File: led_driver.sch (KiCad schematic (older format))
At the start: 3 parts, among them Q3 MMBT5551

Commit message: ready to order?
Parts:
- renumbered Q3 to Q9, R15 to R13
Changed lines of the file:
@@
 AR Path="/620593AE/61D2781A" Ref="Q?"  Part="1"
 AR Path="/61D2781A" Ref="Q?"  Part="1"
-AR Path="/61D242FF/61D2781A" Ref="Q3"  Part="1"
-AR Path="/61D33B82/61D2781A" Ref="Q6"  Part="1"
-F 0 "Q6" V 3035 2000 50  0000 C CNN
+AR Path="/61D242FF/61D2781A" Ref="Q9"  Part="1"
+AR Path="/61D33B82/61D2781A" Ref="Q10"  Part="1"
+F 0 "Q10" V 3035 2000 50  0000 C CNN
 F 1 "MMBT5551" V 3126 2000 50  0000 C CNN
 F 2 "Package_TO_SOT_SMD:SOT-23" H 3000 1925 50  0001 L CIN
@@
 AR Path="/61D27821" Ref="R?"  Part="1"
 AR Path="/61D242FF/61D27821" Ref="R12"  Part="1"
-AR Path="/61D33B82/61D27821" Ref="R16"  Part="1"
-F 0 "R16" V 3157 1800 50  0000 C CNN
+AR Path="/61D33B82/61D27821" Ref="R14"  Part="1"
+F 0 "R14" V 3157 1800 50  0000 C CNN
 F 1 "4.7k" V 3066 1800 50  0000 C CNN
 F 2 "Resistor_SMD:R_0402_1005Metric" V 2880 1800 50  0001 C CNN
@@
 AR Path="/61C031A3/61D27827" Ref="#PWR?"  Part="1"
 AR Path="/61D27827" Ref="#PWR?"  Part="1"
-AR Path="/61D242FF/61D27827" Ref="#PWR04"  Part="1"
-AR Path="/61D33B82/61D27827" Ref="#PWR08"  Part="1"
-F 0 "#PWR08" H 3000 1850 50  0001 C CNN
+AR Path="/61D242FF/61D27827" Ref="#PWR035"  Part="1"
+AR Path="/61D33B82/61D27827" Ref="#PWR036"  Part="1"
+F 0 "#PWR036" H 3000 1850 50  0001 C CNN
 F 1 "GND" V 3005 1972 50  0000 R CNN
 F 2 "" H 3000 2100 50  0001 C CNN
@@
 AR Path="/61C031A3/61D28FF4" Ref="R?"  Part="1"
 AR Path="/61D28FF4" Ref="R?"  Part="1"
-AR Path="/61D242FF/61D28FF4" Ref="R15"  Part="1"
-AR Path="/61D33B82/61D28FF4" Ref="R18"  Part="1"
-F 0 "R18" V 1593 2100 50  0000 C CNN
+AR Path="/61D242FF/61D28FF4" Ref="R13"  Part="1"
+AR Path="/61D33B82/61D28FF4" Ref="R15"  Part="1"
+F 0 "R15" V 1593 2100 50  0000 C CNN
 F 1 "220" V 1684 2100 50  0000 C CNN
 F 2 "Resistor_SMD:R_0402_1005Metric" V 1730 2100 50  0001 C CNN

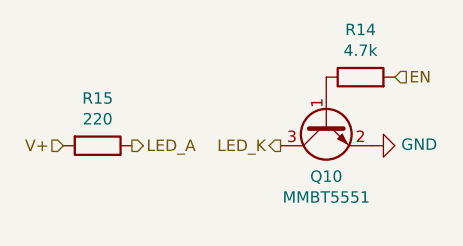
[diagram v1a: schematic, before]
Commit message: we can tolerate higher frequencies as long as our led strips are only a dozen or so metres long
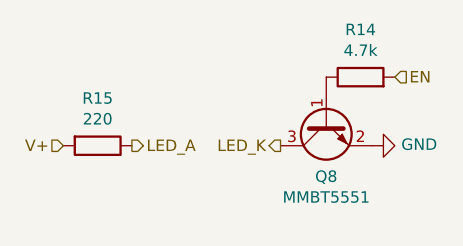
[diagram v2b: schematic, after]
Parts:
- renumbered Q9 to Q7
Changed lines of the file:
@@
 AR Path="/620593AE/61D2781A" Ref="Q?"  Part="1"
 AR Path="/61D2781A" Ref="Q?"  Part="1"
-AR Path="/61D242FF/61D2781A" Ref="Q9"  Part="1"
-AR Path="/61D33B82/61D2781A" Ref="Q10"  Part="1"
-F 0 "Q10" V 3035 2000 50  0000 C CNN
+AR Path="/61D242FF/61D2781A" Ref="Q7"  Part="1"
+AR Path="/61D33B82/61D2781A" Ref="Q8"  Part="1"
+F 0 "Q8" V 3035 2000 50  0000 C CNN
 F 1 "MMBT5551" V 3126 2000 50  0000 C CNN
 F 2 "Package_TO_SOT_SMD:SOT-23" H 3000 1925 50  0001 L CIN
@@
 AR Path="/61C031A3/61D27827" Ref="#PWR?"  Part="1"
 AR Path="/61D27827" Ref="#PWR?"  Part="1"
-AR Path="/61D242FF/61D27827" Ref="#PWR035"  Part="1"
-AR Path="/61D33B82/61D27827" Ref="#PWR036"  Part="1"
-F 0 "#PWR036" H 3000 1850 50  0001 C CNN
+AR Path="/61D242FF/61D27827" Ref="#PWR037"  Part="1"
+AR Path="/61D33B82/61D27827" Ref="#PWR038"  Part="1"
+F 0 "#PWR038" H 3000 1850 50  0001 C CNN
 F 1 "GND" V 3005 1972 50  0000 R CNN
 F 2 "" H 3000 2100 50  0001 C CNN

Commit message: add mosfets, fix led+i2c resistors
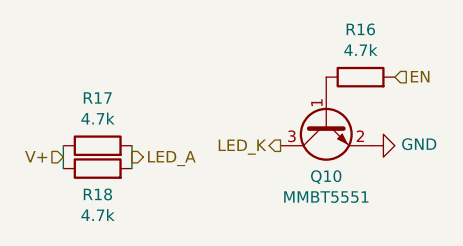
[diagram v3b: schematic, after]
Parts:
- removed R13: 220, Resistor_SMD:R_0402_1005Metric, symbol Device:R
- added R14, R15: 4.7k, Resistor_SMD:R_0402_1005Metric, symbol Device:R
- renumbered Q7 to Q9, R12 to R13
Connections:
- net LED_A: now also R14.2, R15.2
- net V+: now also R14.1, R15.1
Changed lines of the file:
@@
 Text HLabel 3100 1800 2    50   Input ~ 0
 EN
-Text HLabel 1650 2100 0    50   Input ~ 0
+Text HLabel 1650 2150 0    50   Input ~ 0
 V+
-Text HLabel 1950 2100 2    50   Output ~ 0
+Text HLabel 1950 2150 2    50   Output ~ 0
 LED_A
 Text HLabel 2600 2100 0    50   Output ~ 0
@@
 AR Path="/620593AE/61D2781A" Ref="Q?"  Part="1"
 AR Path="/61D2781A" Ref="Q?"  Part="1"
-AR Path="/61D242FF/61D2781A" Ref="Q7"  Part="1"
-AR Path="/61D33B82/61D2781A" Ref="Q8"  Part="1"
-F 0 "Q8" V 3035 2000 50  0000 C CNN
+AR Path="/61D242FF/61D2781A" Ref="Q9"  Part="1"
+AR Path="/61D33B82/61D2781A" Ref="Q10"  Part="1"
+F 0 "Q10" V 3035 2000 50  0000 C CNN
 F 1 "MMBT5551" V 3126 2000 50  0000 C CNN
 F 2 "Package_TO_SOT_SMD:SOT-23" H 3000 1925 50  0001 L CIN
@@
 AR Path="/61C031A3/61D27821" Ref="R?"  Part="1"
 AR Path="/61D27821" Ref="R?"  Part="1"
-AR Path="/61D242FF/61D27821" Ref="R12"  Part="1"
-AR Path="/61D33B82/61D27821" Ref="R14"  Part="1"
-F 0 "R14" V 3157 1800 50  0000 C CNN
+AR Path="/61D242FF/61D27821" Ref="R13"  Part="1"
+AR Path="/61D33B82/61D27821" Ref="R16"  Part="1"
+F 0 "R16" V 3157 1800 50  0000 C CNN
 F 1 "4.7k" V 3066 1800 50  0000 C CNN
 F 2 "Resistor_SMD:R_0402_1005Metric" V 2880 1800 50  0001 C CNN
@@
 AR Path="/61C031A3/61D27827" Ref="#PWR?"  Part="1"
 AR Path="/61D27827" Ref="#PWR?"  Part="1"
-AR Path="/61D242FF/61D27827" Ref="#PWR037"  Part="1"
-AR Path="/61D33B82/61D27827" Ref="#PWR038"  Part="1"
-F 0 "#PWR038" H 3000 1850 50  0001 C CNN
+AR Path="/61D242FF/61D27827" Ref="#PWR039"  Part="1"
+AR Path="/61D33B82/61D27827" Ref="#PWR040"  Part="1"
+F 0 "#PWR040" H 3000 1850 50  0001 C CNN
 F 1 "GND" V 3005 1972 50  0000 R CNN
 F 2 "" H 3000 2100 50  0001 C CNN
@@
 $Comp
 L Device:R R?
-U 1 1 61D28FF4
+U 1 1 6232FC77
 P 1800 2100
-AR Path="/61B5C5B6/61D28FF4" Ref="R?"  Part="1"
-AR Path="/61C03040/61D28FF4" Ref="R?"  Part="1"
-AR Path="/61C031A1/61D28FF4" Ref="R?"  Part="1"
-AR Path="/61C031A3/61D28FF4" Ref="R?"  Part="1"
-AR Path="/61D28FF4" Ref="R?"  Part="1"
-AR Path="/61D242FF/61D28FF4" Ref="R13"  Part="1"
-AR Path="/61D33B82/61D28FF4" Ref="R15"  Part="1"
-F 0 "R15" V 1593 2100 50  0000 C CNN
-F 1 "220" V 1684 2100 50  0000 C CNN
+AR Path="/61B5C5B6/6232FC77" Ref="R?"  Part="1"
+AR Path="/61C03040/6232FC77" Ref="R?"  Part="1"
+AR Path="/61C031A1/6232FC77" Ref="R?"  Part="1"
+AR Path="/61C031A3/6232FC77" Ref="R?"  Part="1"
+AR Path="/6232FC77" Ref="R?"  Part="1"
+AR Path="/61D242FF/6232FC77" Ref="R14"  Part="1"
+AR Path="/61D33B82/6232FC77" Ref="R17"  Part="1"
+F 0 "R17" V 2007 2100 50  0000 C CNN
+F 1 "4.7k" V 1916 2100 50  0000 C CNN
 F 2 "Resistor_SMD:R_0402_1005Metric" V 1730 2100 50  0001 C CNN
 F 3 "~" H 1800 2100 50  0001 C CNN
-F 4 "C25091" H 1800 2100 50  0001 C CNN "JLC"
+F 4 "C25900" H 1800 2100 50  0001 C CNN "JLC"
 	1    1800 2100
-	0    1    1    0
+	0    -1   -1   0
 $EndComp
+$Comp
+L Device:R R?
+U 1 1 623300C4
+P 1800 2200
+AR Path="/61B5C5B6/623300C4" Ref="R?"  Part="1"
+AR Path="/61C03040/623300C4" Ref="R?"  Part="1"
+AR Path="/61C031A1/623300C4" Ref="R?"  Part="1"
+AR Path="/61C031A3/623300C4" Ref="R?"  Part="1"
+AR Path="/623300C4" Ref="R?"  Part="1"
+AR Path="/61D242FF/623300C4" Ref="R15"  Part="1"
+AR Path="/61D33B82/623300C4" Ref="R18"  Part="1"
+F 0 "R18" V 1685 2200 50  0000 C CNN
+F 1 "4.7k" V 1594 2200 50  0000 C CNN
+F 2 "Resistor_SMD:R_0402_1005Metric" V 1730 2200 50  0001 C CNN
+F 3 "~" H 1800 2200 50  0001 C CNN
+F 4 "C25900" H 1800 2200 50  0001 C CNN "JLC"
+	1    1800 2200
+	0    -1   -1   0
+$EndComp
+Wire Wire Line
+	1950 2200 1950 2100
+Wire Wire Line
+	1650 2100 1650 2200
 $EndSCHEMATC

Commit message: swapped placement for 5V LDO vs LEDs, for more stable 5V supply when power-side of ground is noisy
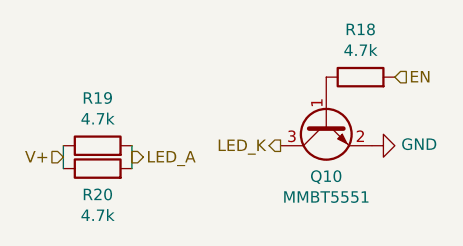
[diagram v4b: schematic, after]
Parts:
- renumbered R13 to R15, R14 to R16, R15 to R17
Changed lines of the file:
@@
 AR Path="/61C031A3/61D27821" Ref="R?"  Part="1"
 AR Path="/61D27821" Ref="R?"  Part="1"
-AR Path="/61D242FF/61D27821" Ref="R13"  Part="1"
-AR Path="/61D33B82/61D27821" Ref="R16"  Part="1"
-F 0 "R16" V 3157 1800 50  0000 C CNN
+AR Path="/61D242FF/61D27821" Ref="R15"  Part="1"
+AR Path="/61D33B82/61D27821" Ref="R18"  Part="1"
+F 0 "R18" V 3157 1800 50  0000 C CNN
 F 1 "4.7k" V 3066 1800 50  0000 C CNN
 F 2 "Resistor_SMD:R_0402_1005Metric" V 2880 1800 50  0001 C CNN
@@
 AR Path="/61C031A3/6232FC77" Ref="R?"  Part="1"
 AR Path="/6232FC77" Ref="R?"  Part="1"
-AR Path="/61D242FF/6232FC77" Ref="R14"  Part="1"
-AR Path="/61D33B82/6232FC77" Ref="R17"  Part="1"
-F 0 "R17" V 2007 2100 50  0000 C CNN
+AR Path="/61D242FF/6232FC77" Ref="R16"  Part="1"
+AR Path="/61D33B82/6232FC77" Ref="R19"  Part="1"
+F 0 "R19" V 2007 2100 50  0000 C CNN
 F 1 "4.7k" V 1916 2100 50  0000 C CNN
 F 2 "Resistor_SMD:R_0402_1005Metric" V 1730 2100 50  0001 C CNN
@@
 AR Path="/61C031A3/623300C4" Ref="R?"  Part="1"
 AR Path="/623300C4" Ref="R?"  Part="1"
-AR Path="/61D242FF/623300C4" Ref="R15"  Part="1"
-AR Path="/61D33B82/623300C4" Ref="R18"  Part="1"
-F 0 "R18" V 1685 2200 50  0000 C CNN
+AR Path="/61D242FF/623300C4" Ref="R17"  Part="1"
+AR Path="/61D33B82/623300C4" Ref="R20"  Part="1"
+F 0 "R20" V 1685 2200 50  0000 C CNN
 F 1 "4.7k" V 1594 2200 50  0000 C CNN
 F 2 "Resistor_SMD:R_0402_1005Metric" V 1730 2200 50  0001 C CNN

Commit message: order ready
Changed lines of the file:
@@
 AR Path="/61D242FF/61D2781A" Ref="Q9"  Part="1"
 AR Path="/61D33B82/61D2781A" Ref="Q10"  Part="1"
-F 0 "Q10" V 3035 2000 50  0000 C CNN
+F 0 "Q9" V 3035 2000 50  0000 C CNN
 F 1 "MMBT5551" V 3126 2000 50  0000 C CNN
 F 2 "Package_TO_SOT_SMD:SOT-23" H 3000 1925 50  0001 L CIN
@@
 AR Path="/61D242FF/61D27821" Ref="R15"  Part="1"
 AR Path="/61D33B82/61D27821" Ref="R18"  Part="1"
-F 0 "R18" V 3157 1800 50  0000 C CNN
+F 0 "R15" V 3157 1800 50  0000 C CNN
 F 1 "4.7k" V 3066 1800 50  0000 C CNN
 F 2 "Resistor_SMD:R_0402_1005Metric" V 2880 1800 50  0001 C CNN
@@
 AR Path="/61D242FF/61D27827" Ref="#PWR039"  Part="1"
 AR Path="/61D33B82/61D27827" Ref="#PWR040"  Part="1"
-F 0 "#PWR040" H 3000 1850 50  0001 C CNN
+F 0 "#PWR039" H 3000 1850 50  0001 C CNN
 F 1 "GND" V 3005 1972 50  0000 R CNN
 F 2 "" H 3000 2100 50  0001 C CNN
@@
 AR Path="/61D242FF/6232FC77" Ref="R16"  Part="1"
 AR Path="/61D33B82/6232FC77" Ref="R19"  Part="1"
-F 0 "R19" V 2007 2100 50  0000 C CNN
+F 0 "R16" V 2007 2100 50  0000 C CNN
 F 1 "4.7k" V 1916 2100 50  0000 C CNN
 F 2 "Resistor_SMD:R_0402_1005Metric" V 1730 2100 50  0001 C CNN
@@
 AR Path="/61D242FF/623300C4" Ref="R17"  Part="1"
 AR Path="/61D33B82/623300C4" Ref="R20"  Part="1"
-F 0 "R20" V 1685 2200 50  0000 C CNN
+F 0 "R17" V 1685 2200 50  0000 C CNN
 F 1 "4.7k" V 1594 2200 50  0000 C CNN
 F 2 "Resistor_SMD:R_0402_1005Metric" V 1730 2200 50  0001 C CNN

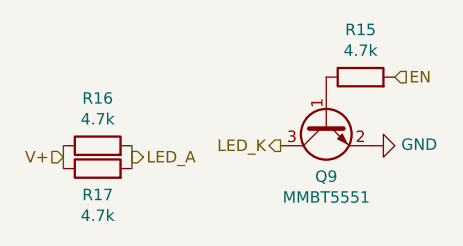
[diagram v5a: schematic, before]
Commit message: exposed NRST
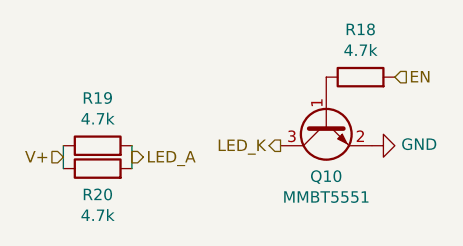
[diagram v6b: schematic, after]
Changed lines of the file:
@@
 AR Path="/61D242FF/61D2781A" Ref="Q9"  Part="1"
 AR Path="/61D33B82/61D2781A" Ref="Q10"  Part="1"
-F 0 "Q9" V 3035 2000 50  0000 C CNN
+F 0 "Q10" V 3035 2000 50  0000 C CNN
 F 1 "MMBT5551" V 3126 2000 50  0000 C CNN
 F 2 "Package_TO_SOT_SMD:SOT-23" H 3000 1925 50  0001 L CIN
@@
 AR Path="/61D242FF/61D27821" Ref="R15"  Part="1"
 AR Path="/61D33B82/61D27821" Ref="R18"  Part="1"
-F 0 "R15" V 3157 1800 50  0000 C CNN
+F 0 "R18" V 3157 1800 50  0000 C CNN
 F 1 "4.7k" V 3066 1800 50  0000 C CNN
 F 2 "Resistor_SMD:R_0402_1005Metric" V 2880 1800 50  0001 C CNN
@@
 AR Path="/61C031A3/61D27827" Ref="#PWR?"  Part="1"
 AR Path="/61D27827" Ref="#PWR?"  Part="1"
-AR Path="/61D242FF/61D27827" Ref="#PWR039"  Part="1"
-AR Path="/61D33B82/61D27827" Ref="#PWR040"  Part="1"
+AR Path="/61D242FF/61D27827" Ref="#PWR038"  Part="1"
+AR Path="/61D33B82/61D27827" Ref="#PWR039"  Part="1"
 F 0 "#PWR039" H 3000 1850 50  0001 C CNN
 F 1 "GND" V 3005 1972 50  0000 R CNN
@@
 AR Path="/61D242FF/6232FC77" Ref="R16"  Part="1"
 AR Path="/61D33B82/6232FC77" Ref="R19"  Part="1"
-F 0 "R16" V 2007 2100 50  0000 C CNN
+F 0 "R19" V 2007 2100 50  0000 C CNN
 F 1 "4.7k" V 1916 2100 50  0000 C CNN
 F 2 "Resistor_SMD:R_0402_1005Metric" V 1730 2100 50  0001 C CNN
@@
 AR Path="/61D242FF/623300C4" Ref="R17"  Part="1"
 AR Path="/61D33B82/623300C4" Ref="R20"  Part="1"
-F 0 "R17" V 1685 2200 50  0000 C CNN
+F 0 "R20" V 1685 2200 50  0000 C CNN
 F 1 "4.7k" V 1594 2200 50  0000 C CNN
 F 2 "Resistor_SMD:R_0402_1005Metric" V 1730 2200 50  0001 C CNN
